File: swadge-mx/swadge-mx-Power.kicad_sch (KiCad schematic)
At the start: 28 parts, among them U10 M3410, U11 AW32001ECSR, U9 BQ24073RGT

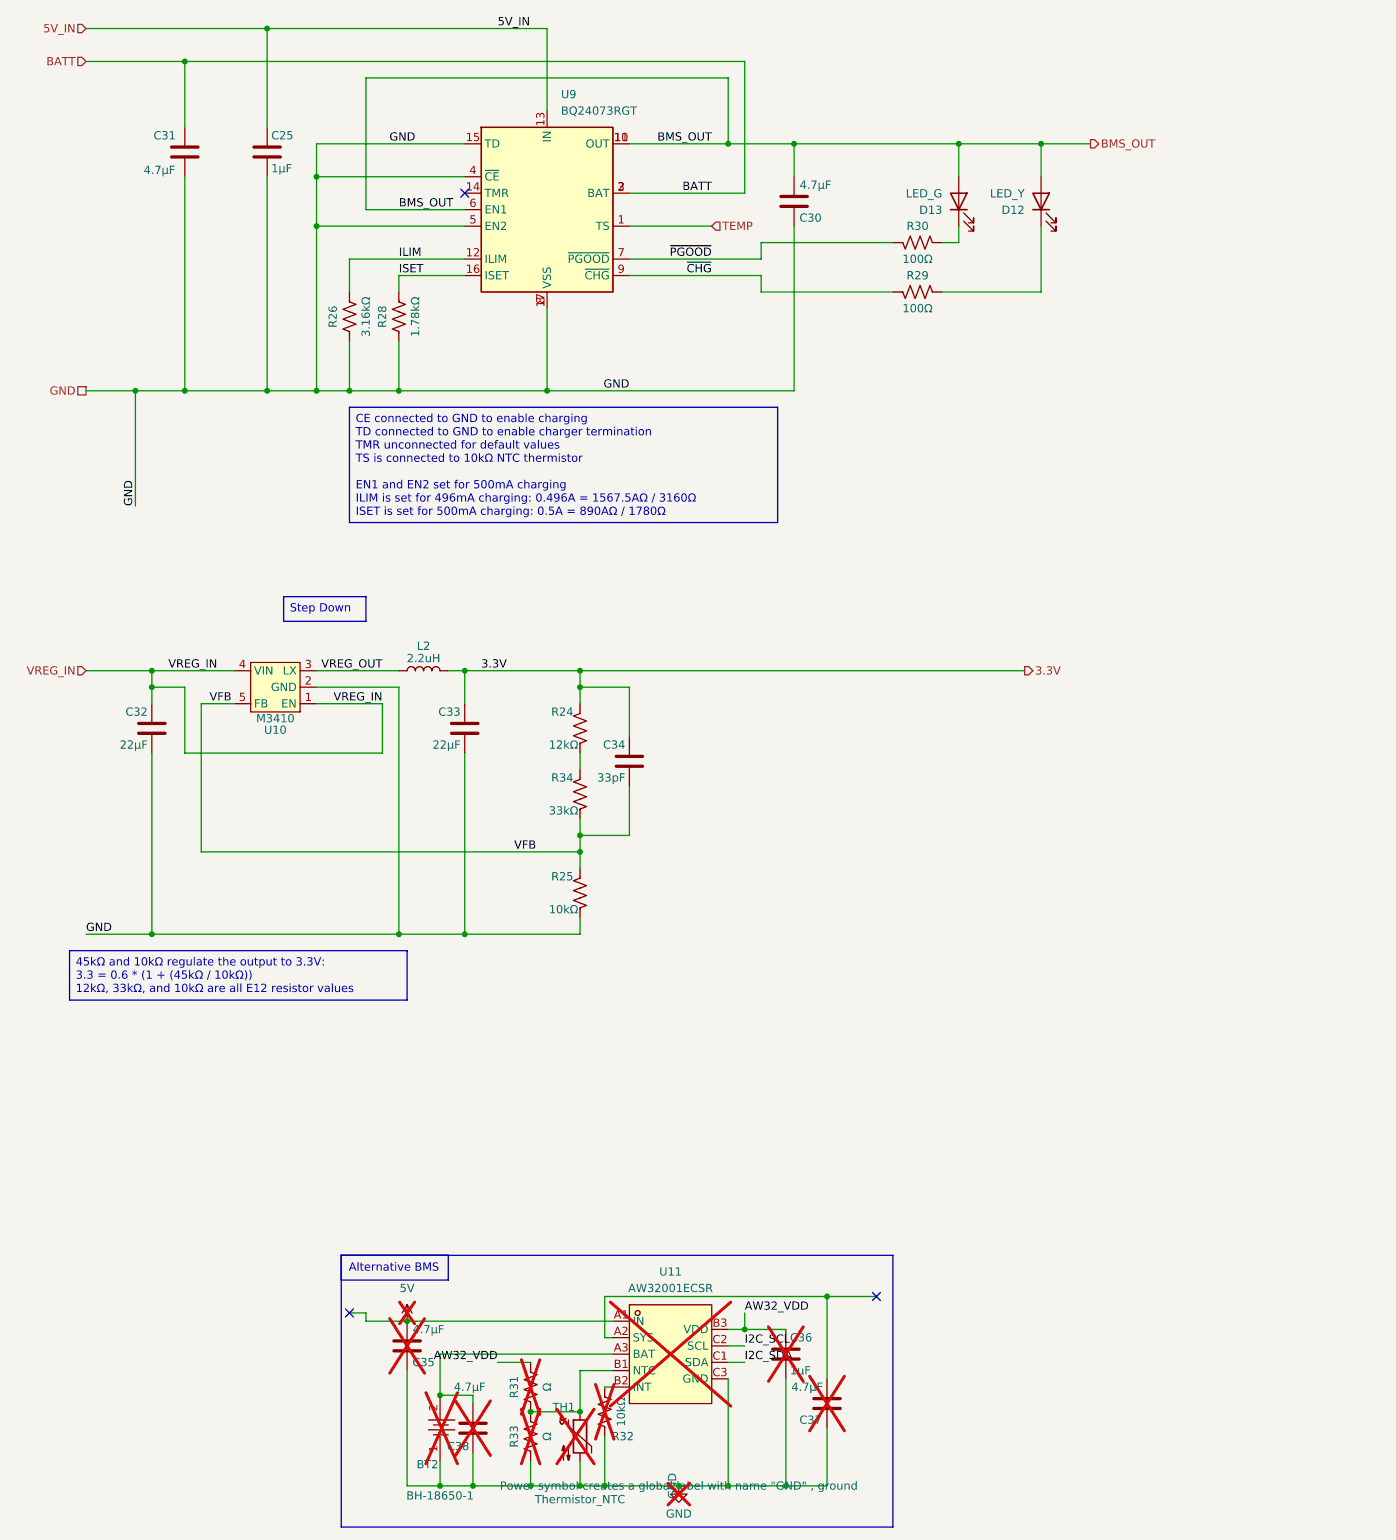
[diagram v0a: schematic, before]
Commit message: Further Subdivide Sheets
Moved all audio into one sheet, and sub-divided into DAC and amp sheets. Moved all power into one sheet and sub-divided into BMS and Buck.
Cleaned up front page a bit.
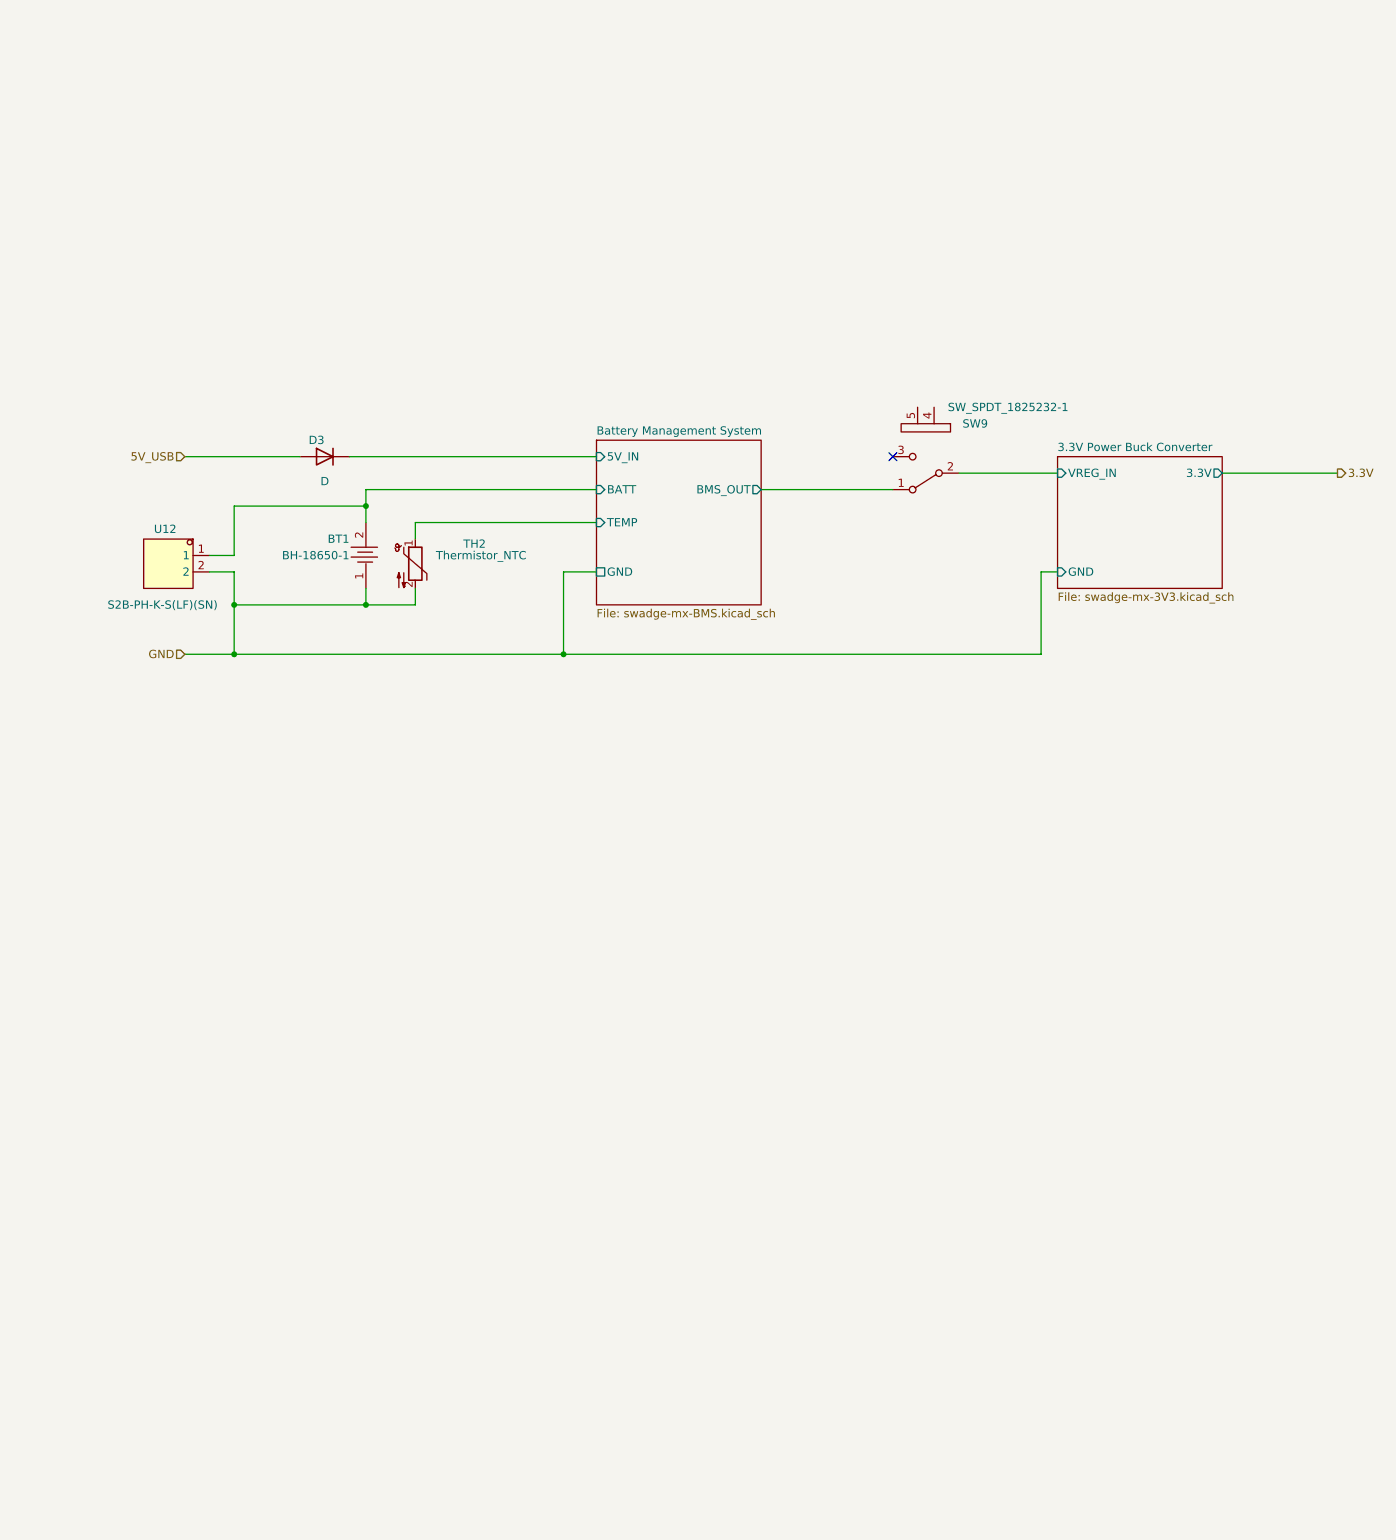
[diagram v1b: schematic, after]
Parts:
- removed BT2: BH-18650-1, Swadge_Parts:BAT-TH_BH-18650-A1AJ005, symbol Swadge_Parts:BH-18650-1
- removed C25, C36: 1μF, Swadge_Parts:C_0603_1608Metric, symbol Swadge_Parts:C
- removed C30, C31, C35, C37, C38: 4.7μF, Swadge_Parts:C_0603_1608Metric, symbol Swadge_Parts:C
- removed C32, C33: 22μF, Swadge_Parts:C_0603_1608Metric, symbol Swadge_Parts:C
- removed C34: 33pF, Swadge_Parts:C_0603_1608Metric, symbol Swadge_Parts:C
- removed D12: LED_Y, Swadge_Parts:LED_0603_1608Metric, symbol Swadge_Parts:LED
- removed D13: LED_G, Swadge_Parts:LED_0603_1608Metric, symbol Swadge_Parts:LED
- removed L2: 2.2uH, Swadge_Parts:L_1008_2520Metric, symbol Swadge_Parts:L
- removed R24: 12kΩ, Swadge_Parts:R_0603_1608Metric, symbol Swadge_Parts:R_US
- removed R25, R32: 10kΩ, Swadge_Parts:R_0603_1608Metric, symbol Swadge_Parts:R_US
- removed R26: 3.16kΩ, Swadge_Parts:R_0603_1608Metric, symbol Swadge_Parts:R_US
- removed R28: 1.78kΩ, Swadge_Parts:R_0603_1608Metric, symbol Swadge_Parts:R_US
- removed R29, R30: 100Ω, Swadge_Parts:R_0603_1608Metric, symbol Swadge_Parts:R_US
- removed R31, R33: Ω, Swadge_Parts:R_0603_1608Metric, symbol Swadge_Parts:R_US
- removed R34: 33kΩ, Swadge_Parts:R_0603_1608Metric, symbol Swadge_Parts:R_US
- removed TH1: Thermistor_NTC, symbol Swadge_Parts:Thermistor_NTC
- removed U10: M3410, Swadge_Parts:SOT-23-5, symbol Swadge_Parts:M3410
- removed U11: AW32001ECSR, Swadge_Parts:WLCSP-9_L1.7-W1.7-R3-C3-P0.50-TL, symbol Swadge_Parts:AW32001ECSR
- removed U9: BQ24073RGT, Swadge_Parts:VQFN-16-1EP_3x3mm_P0.5mm_EP1.6x1.6mm, symbol Swadge_Parts:BQ24073RGT
- added BT1: BH-18650-1, Swadge_Parts:BAT-TH_BH-18650-A1AJ005, symbol Swadge_Parts:BH-18650-1
- added D3: D, Swadge_Parts:D_SMA, symbol Swadge_Parts:D
- added SW9: SW_SPDT_1825232-1, Swadge_Parts:1825232-1, symbol Swadge_Parts:SW_SPDT_1825232-1
- added TH2: Thermistor_NTC, Swadge_Parts:R_0603_1608Metric, symbol Swadge_Parts:Thermistor_NTC
- added U12: S2B-PH-K-S(LF)(SN), Swadge_Parts:CONN-TH_S2B-PH-K-S-LF-SN, symbol Swadge_Parts:S2B-PH-K-S(LF)(SN)
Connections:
- net GND: now also BT1.1, TH2.2, U12.2
- new net 3.3V Power Buck Converter/VREG_IN: SW9.2 (B)
- new net 5V_USB: D3.2 (A)
- new net Battery Management System/5V_IN: D3.1 (K)
- new net Battery Management System/BATT: BT1.2, U12.1
- new net Battery Management System/BMS_OUT: SW9.1 (A)
- new net Battery Management System/TEMP: TH2.1
- no-connect marks 3 -> 1
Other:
- added sheet 3.3V Power Buck Converter (swadge-mx-3V3.kicad_sch)
- added sheet Battery Management System (swadge-mx-BMS.kicad_sch)
- note removed: "Alternative BMS"

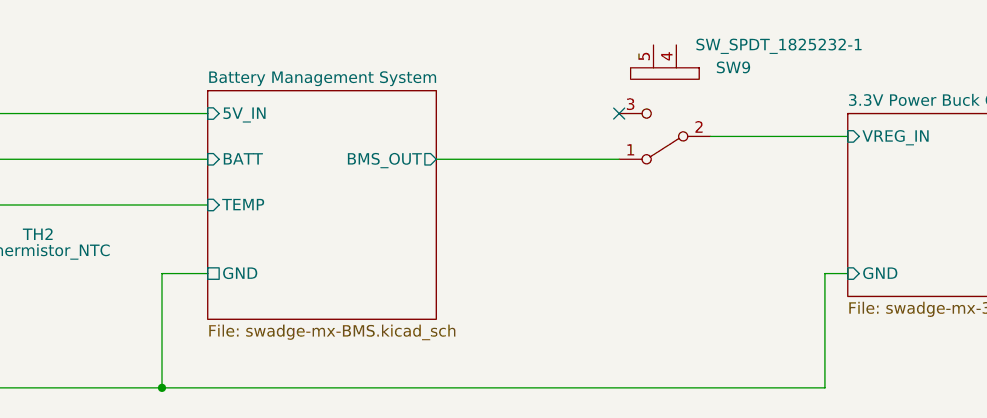
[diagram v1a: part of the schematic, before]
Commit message: Fix SW9 losing its grounded stud
Fixes an issue introduced with previous merge.
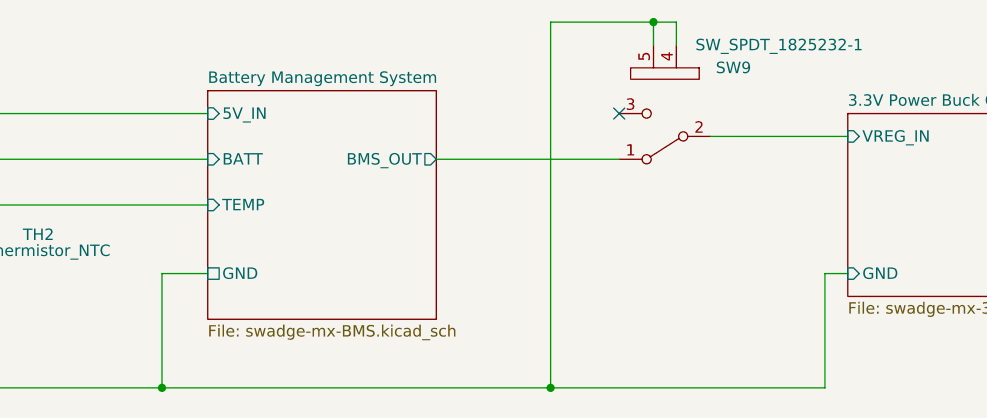
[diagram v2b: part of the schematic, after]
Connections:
- net GND: now also SW9.4 (D), SW9.5 (E)
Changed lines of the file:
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@@
+	)
+	(junction
+		(at 152.4 127)
+		(diameter 0)
+		(color 0 0 0 0)
 	)
 	(junction
@@
 		(color 0 0 0 0)
 	)
+	(junction
+		(at 163.83 86.36)
+		(diameter 0)
+		(color 0 0 0 0)
+	)
 	(no_connect
 		(at 160.02 96.52)
@@
 	(wire
 		(pts
-			(xy 182.88 127) (xy 109.22 127)
+			(xy 182.88 127) (xy 152.4 127)
 		)
 		(stroke
@@
 	(wire
 		(pts
+			(xy 163.83 86.36) (xy 163.83 88.9)
+		)
+		(stroke
+			(width 0)
+			(type default)
+		)
+	)
+	(wire
+		(pts
 			(xy 58.42 119.38) (xy 58.42 114.3)
 		)
@@
 	(wire
 		(pts
+			(xy 163.83 86.36) (xy 152.4 86.36)
+		)
+		(stroke
+			(width 0)
+			(type default)
+		)
+	)
+	(wire
+		(pts
 			(xy 58.42 127) (xy 58.42 119.38)
 		)
@@
 		)
 		(stroke
+			(width 0)
+			(type default)
+		)
+	)
+	(wire
+		(pts
+			(xy 152.4 127) (xy 109.22 127)
+		)
+		(stroke
+			(width 0)
+			(type default)
+		)
+	)
+	(wire
+		(pts
+			(xy 166.37 88.9) (xy 166.37 86.36)
+		)
+		(stroke
+			(width 0)
+			(type default)
+		)
+	)
+	(wire
+		(pts
+			(xy 152.4 86.36) (xy 152.4 127)
+		)
+		(stroke
+			(width 0)
+			(type default)
+		)
+	)
+	(wire
+		(pts
+			(xy 166.37 86.36) (xy 163.83 86.36)
+		)
+		(stroke
